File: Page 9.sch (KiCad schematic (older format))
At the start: 7 parts, among them U801 MCP7940N-xSN, Y801 32.7680 kHz

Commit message: Updates
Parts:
- C801: Mftr Part No. (none) -> Yageo CC0603KPX7R7BB104
- C802, C803: DigiKey Part No. (none) -> 399-7816-1-ND; Mftr Part No. (none) -> Kemet C0603C100J1GACTU
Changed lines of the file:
@@
 F 2 "Capacitor_SMD:C_0603_1608Metric_Pad1.05x0.95mm_HandSolder" H 7188 3600 50  0001 C CNN
 F 3 "~" H 7150 3750 50  0001 C CNN
+F 4 "399-7816-1-ND" H 7150 3750 50  0001 C CNN "DigiKey Part No."
+F 5 "Kemet C0603C100J1GACTU" H 7150 3750 50  0001 C CNN "Mftr Part No."
 	1    7150 3750
 	0    1    1    0
@@
 F 2 "Capacitor_SMD:C_0603_1608Metric_Pad1.05x0.95mm_HandSolder" H 7188 4200 50  0001 C CNN
 F 3 "~" H 7150 4350 50  0001 C CNN
+F 4 "399-7816-1-ND" H 7150 4350 50  0001 C CNN "DigiKey Part No."
+F 5 "Kemet C0603C100J1GACTU" H 7150 4350 50  0001 C CNN "Mftr Part No."
 	1    7150 4350
 	0    1    1    0
@@
 F 2 "Capacitor_SMD:C_0603_1608Metric_Pad1.05x0.95mm_HandSolder" H 4538 3000 50  0001 C CNN
 F 3 "https://www.yageo.com/upload/media/product/productsearch/datasheet/mlcc/UPY-GPHC_X7R_6.3V-to-50V_18.pdf" H 4500 3150 50  0001 C CNN
+F 4 "Yageo CC0603KPX7R7BB104" H 4500 3150 50  0001 C CNN "Mftr Part No."
 	1    4500 3150
 	1    0    0    -1

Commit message: Updates
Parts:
- removed B801: BK-883, Name Plate Class Project:BAT_BK-883, symbol Name~Plate~Class~Library:BK-883
- removed C801: 0.1uF, Capacitor_SMD:C_0603_1608Metric_Pad1.05x0.95mm_HandSolder, symbol Device:C
- removed C802, C803: 10pF, Capacitor_SMD:C_0603_1608Metric_Pad1.05x0.95mm_HandSolder, symbol Device:C
- removed R801: 10k0, Resistor_SMD:R_0603_1608Metric_Pad1.05x0.95mm_HandSolder, symbol Device:R
- removed U801: MCP7940N-xSN, Package_SO:SOIC-8_3.9x4.9mm_P1.27mm, symbol Timer:MCP7940N-xSN
- removed Y801: 32.7680 kHz, Name Plate Class Project:Oscillator_MC-405_32.7680K-D__ROHS, symbol Name~Plate~Class~Library:Oscillator_MC-405_32.7680K-D__ROHS
- added C901: 0.1uF, Capacitor_SMD:C_0603_1608Metric_Pad1.05x0.95mm_HandSolder, symbol Device:C
- added LCD1: LCD 2.4\", Name Plate Class Project:LCD_ER-TFTM024-3, symbol Name~Plate~Class~Library:LCD_ER-TFTM024-3
- added R901, R902, R903, R904, R905, R906: R22K0, Resistor_SMD:R_0603_1608Metric_Pad1.05x0.95mm_HandSolder, symbol Device:R
- added TP901: TP_SPI_MISO, Connector_Wire:SolderWirePad_1x01_SMD_5x10mm, symbol Connector:TestPoint
- added TP902: TP_FONT_nSELECT, Connector_Wire:SolderWirePad_1x01_SMD_5x10mm, symbol Connector:TestPoint
- added TP903: TP_SPI_CLK, Connector_Wire:SolderWirePad_1x01_SMD_5x10mm, symbol Connector:TestPoint
- added TP904: TP_SPI_MOSI, Connector_Wire:SolderWirePad_1x01_SMD_5x10mm, symbol Connector:TestPoint
- added TP905: TP_DC, Connector_Wire:SolderWirePad_1x01_SMD_5x10mm, symbol Connector:TestPoint
- added TP906: TP_LCD_nCS, Connector_Wire:SolderWirePad_1x01_SMD_5x10mm, symbol Connector:TestPoint
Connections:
- net labels added: LCD_CLK, LCD_DC, LCD_FONT_nCS, LCD_FONT_nSELECT, LCD_SPI_CLK, LCD_SPI_MISO, LCD_SPI_MOSI, LCD_nCS, SPI_CLK, SPI_MISO, SPI_MOSI
- net labels removed: RTC_INT, SCL, SDA
- wire segments 29 -> 39
- no-connect marks 0 -> 27
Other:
- note removed: "Real Time Clock"

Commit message: Updates
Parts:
- C901: Mftr Part No. (none) -> Yageo CC0603KPX7R7BB104
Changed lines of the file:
@@
 F 2 "Capacitor_SMD:C_0603_1608Metric_Pad1.05x0.95mm_HandSolder" H 8288 1400 50  0001 C CNN
 F 3 "https://www.yageo.com/upload/media/product/productsearch/datasheet/mlcc/UPY-GPHC_X7R_6.3V-to-50V_18.pdf" H 8250 1550 50  0001 C CNN
+F 4 "Yageo CC0603KPX7R7BB104" H 8250 1550 50  0001 C CNN "Mftr Part No."
 	1    8250 1550
 	1    0    0    -1

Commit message: Updates
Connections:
- net labels removed: LCD_CLK
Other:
- note added: "LCD Screen"
- moved on the sheet: C901, R901, R902, R903, R904, R905, R906, TP901, TP902, TP903, TP904, TP905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

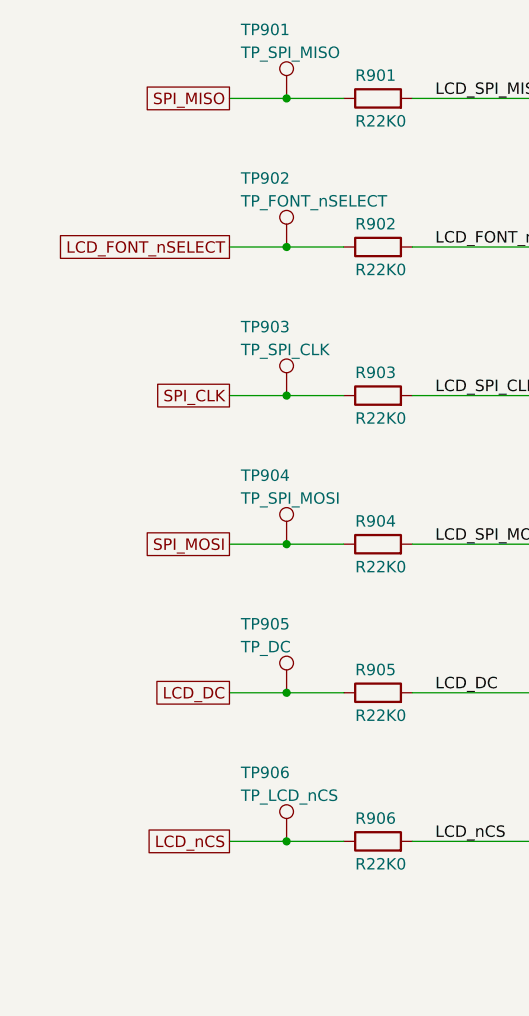
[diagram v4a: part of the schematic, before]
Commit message: Switched to Hierarchical
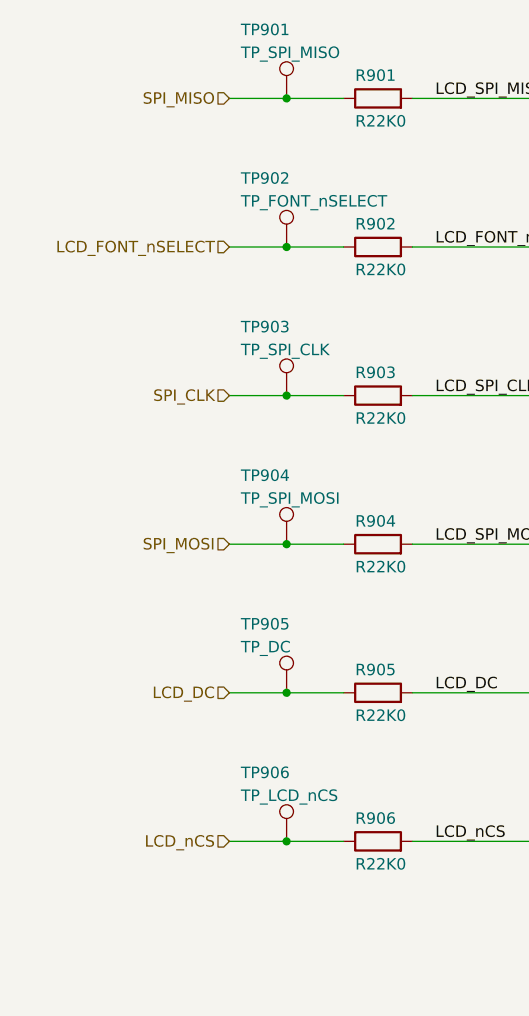
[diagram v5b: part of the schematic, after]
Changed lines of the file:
@@
 $Descr A4 11693 8268
 encoding utf-8
-Sheet 10 10
+Sheet 9 10
 Title ""
 Date ""
@@
 Text Label 4150 2300 0    50   ~ 0
 LCD_SPI_MISO
-Text GLabel 3250 2300 0    50   UnSpc ~ 0
-SPI_MISO
 Wire Wire Line
 	4050 2950 4750 2950
@@
 Text Label 4150 2950 0    50   ~ 0
 LCD_FONT_nCS
-Text GLabel 3250 2950 0    50   UnSpc ~ 0
-LCD_FONT_nSELECT
 Wire Wire Line
 	4050 3600 4750 3600
@@
 Text Label 4150 4250 0    50   ~ 0
 LCD_SPI_MOSI
-Text GLabel 3250 4250 0    50   UnSpc ~ 0
-SPI_MOSI
 Wire Wire Line
 	4050 4900 4750 4900
@@
 Text Label 4150 4900 0    50   ~ 0
 LCD_DC
-Text GLabel 3250 4900 0    50   UnSpc ~ 0
-LCD_DC
 Wire Wire Line
 	4050 5550 4750 5550
@@
 Text Label 4150 5550 0    50   ~ 0
 LCD_nCS
-Text GLabel 3250 5550 0    50   UnSpc ~ 0
-LCD_nCS
-Text GLabel 3250 3600 0    50   UnSpc ~ 0
-SPI_CLK
 $Comp
 L Connector:TestPoint TP906
@@
 Text Notes 5050 6250 0    98   ~ 20
 LCD Screen
+Text HLabel 3250 2300 0    50   Input ~ 0
+SPI_MISO
+Text HLabel 3250 2950 0    50   Input ~ 0
+LCD_FONT_nSELECT
+Text HLabel 3250 3600 0    50   Input ~ 0
+SPI_CLK
+Text HLabel 3250 4250 0    50   Input ~ 0
+SPI_MOSI
+Text HLabel 3250 4900 0    50   Input ~ 0
+LCD_DC
+Text HLabel 3250 5550 0    50   Input ~ 0
+LCD_nCS
 $EndSCHEMATC
